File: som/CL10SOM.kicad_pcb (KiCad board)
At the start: 4 copper layers, 34 x 32 mm, 54 parts, among them IC1 10CL025YU256C8G, J1 Conn_01x02_Pin, U1 MT46H32M16LFBF-5 IT:C, U2 MX25L12833FM2, U6 AT93C46DN-SH-T, U7 SG3225CAN 50.0000M-TJGA6, X1 DF40C-120DS-0.4V51

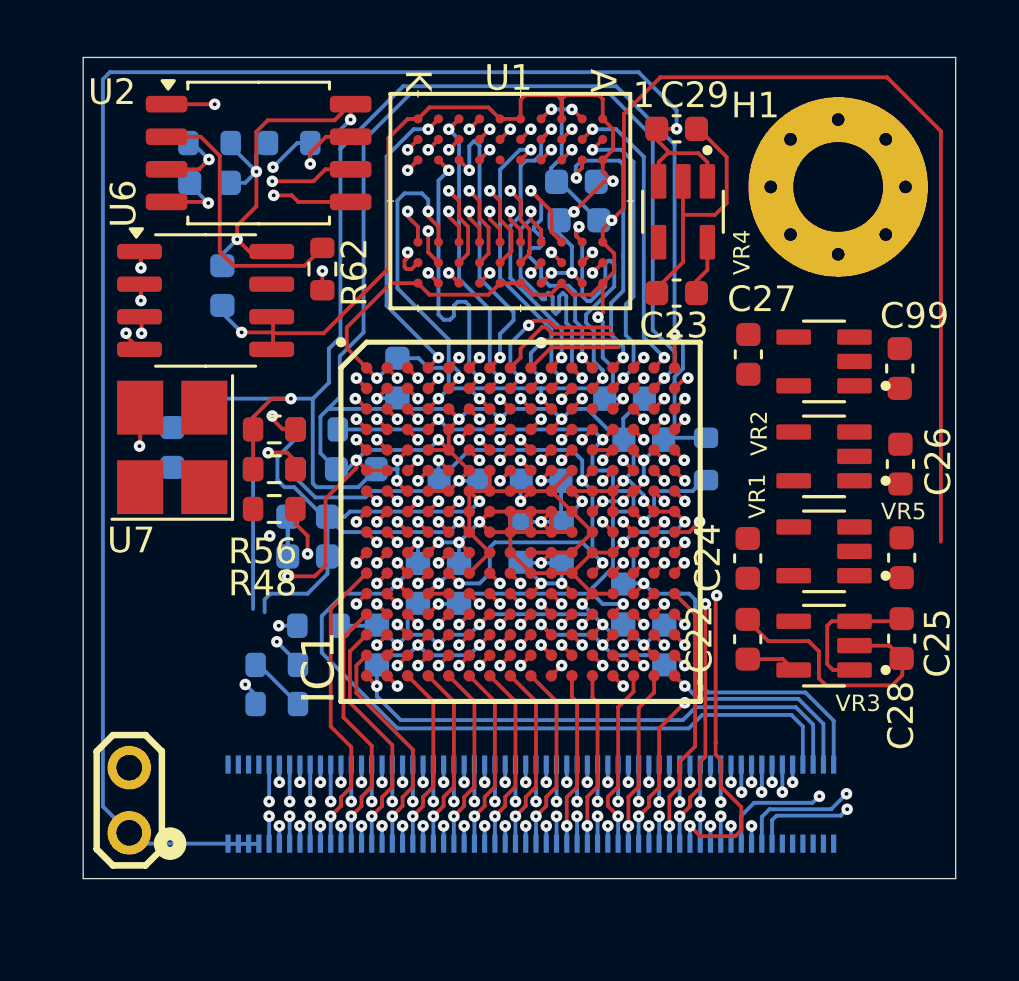
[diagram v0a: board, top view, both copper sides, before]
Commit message: Use switching regulators for 3v3 and 1v2
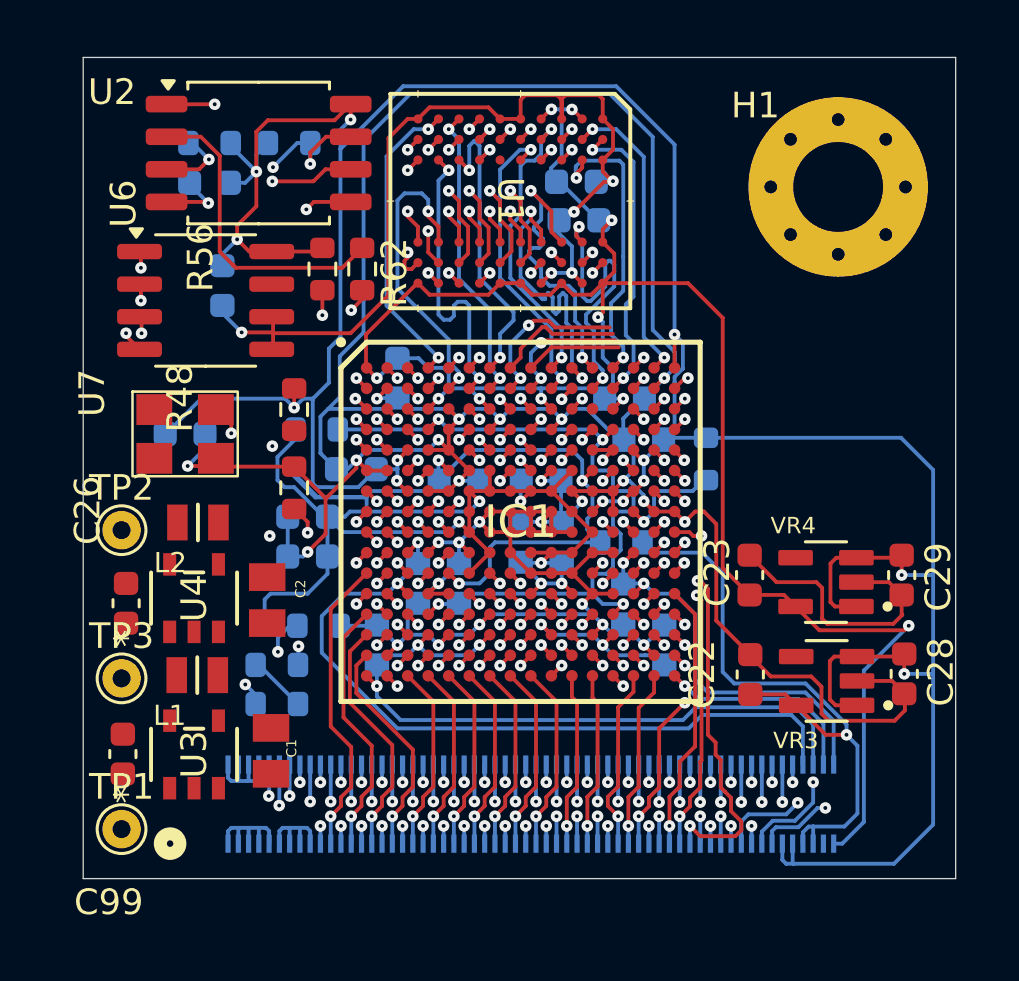
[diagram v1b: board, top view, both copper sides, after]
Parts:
- removed C24, C25, C27: 2.2uF, Capacitor_SMD:C_0603_1608Metric
- removed J1: Conn_01x02_Pin, Library:JUMPER_1
- removed VR1, VR5: AP7366EA-33W5-7, Library:SOT95P285X140-5N
- removed VR2: AP7366EA-12W5-7, Library:SOT95P285X140-5N
- added C1: GRM21BR60J226ME39L, Library:CAPC2012X140N, F.Cu at (90.6, 71.4)
- added C2: GRM21BR60J226ME39L, Library:CAPC2012X140N, F.Cu at (90.5, 65.5)
- added L1: MURATA_DFE21CCN1R0MELL, Library:MURATA_DFE21CCN1R0MELL_0, F.Cu at (87.8, 68.5)
- added L2: MURATA_DFE21CCN1R0MELL, Library:MURATA_DFE21CCN1R0MELL_0, F.Cu at (87.8, 62.5)
- added TP1: TestPoint, TestPoint:TestPoint_THTPad_D1.5mm_Drill0.7mm, F.Cu at (84.8, 74.5)
- added TP2: TestPoint, TestPoint:TestPoint_THTPad_D1.5mm_Drill0.7mm, F.Cu at (84.8, 62.8)
- added TP3: TestPoint, TestPoint:TestPoint_THTPad_D1.5mm_Drill0.7mm, F.Cu at (84.8, 68.6)
- added U3: SC189ZSKTRT, Library:SOT23-5-SC189_SEM, F.Cu at (87.6, 71.6)
- added U4: SC189CSKTRT, Library:SOT_CSKTRT_SEM, F.Cu at (87.6, 65.5)
- C26, C99: value 2.2uF -> 4.7uF
- moved C99 32.3 mm to (84.8, 71.5), turned to -90 degrees
- moved C26 31.5 mm to (85.0, 65.7), turned to -90 degrees
- moved C29 19.5 mm to (115.2, 64.6), turned to 90 degrees
- moved VR4 15.5 mm to (112.2, 64.8), turned to 180 degrees
- moved R44 13.8 mm to (104.3, 63.3), turned to 180 degrees
- moved C23 11.4 mm to (109.3, 64.6), turned to -90 degrees
- moved R56 6.53 mm to (92.6, 52.6), turned to -90 degrees
- moved R48 2.45 mm to (91.5, 58.1), turned to -90 degrees
- moved R62 1.55 mm to (94.2, 52.6)
- moved VR3 1.38 mm to (112.3, 68.7)
- moved C22 1.38 mm to (109.3, 68.5)
- moved C28 1.38 mm to (115.3, 68.4)
- moved R46 1.13 mm to (91.5, 61.2), turned to -90 degrees
- moved C9 0.73 mm to (87.3, 59.1), turned to 180 degrees
- moved U7 0.72 mm to (87.3, 59.1), turned to 0 degrees
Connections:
- C26 pad 2: Net-(VR1-OUT) -> +5V
- C28 pad 2: +5V -> +3V3
- C29 pad 2: +5V -> +3V3
- VR3 pad 1: +5V -> +3V3
- VR3 pad 3: +5V -> +3V3
- VR4 pad 1: +5V -> +3V3
- VR4 pad 3: +5V -> +3V3
- X1 pad 10: /TCK -> /TDI
- X1 pad 109: +3.3V -> +3V3
- X1 pad 11: /TMS -> +3V3
- X1 pad 111: +3.3V -> +3V3
- X1 pad 12: /TDO -> /TCK
- X1 pad 13: unconnected-(X1-Pad13) -> +3V3
- X1 pad 14: unconnected-(X1-Pad14) -> /TMS
- X1 pad 15: unconnected-(X1-Pad15) -> +3V3
- X1 pad 16: unconnected-(X1-Pad16) -> /TDO
- X1 pad 17: unconnected-(X1-Pad17) -> +3V3
- X1 pad 9: /TDI -> +5V
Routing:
- net +5V: track 70.0 -> 4.54 mm, vias 1 -> 0
- net +3V3: track 82.9 -> 131.8 mm, vias 11 -> 13
- net +2V5: track 7.42 -> 24.7 mm, vias 0 -> 1
- net GND: track 206.1 -> 219.2 mm
- net /B5-IO7p: track 18.7 -> 13.6 mm
- net /B5-IO8p: track 19.7 -> 14.7 mm
- net /B5-IO9n: track 20.5 -> 15.5 mm
- net /B5-IO7n: track 17.6 -> 12.8 mm
- net /B5-IO8n: track 19.3 -> 14.7 mm
- net +1V8: track 80.1 -> 75.8 mm, vias 9 -> 10
- net /CLC50: track 11.8 -> 7.80 mm
- net /B5-IO10: track 24.0 -> 20.8 mm
- net PLLA: track 26.6 -> 29.7 mm
- net /B5-IO11: track 26.3 -> 23.2 mm
- net /B6-IO7: track 21.4 -> 18.4 mm
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
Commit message: All routed, no errors
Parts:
- added C10: 100nF, Capacitor_SMD:C_0603_1608Metric, B.Cu at (110.7, 55.6)
- added C19: 100nF, Capacitor_SMD:C_0603_1608Metric, F.Cu at (108.8, 68.0)
- added C24: 100nF, Capacitor_SMD:C_0603_1608Metric, F.Cu at (110.3, 68.0)
- added C25: 100nF, Capacitor_SMD:C_0603_1608Metric, F.Cu at (111.8, 68.0)
- added C27: 100nF, Capacitor_SMD:C_0603_1608Metric, F.Cu at (113.4, 68.0)
- added TP4: TestPoint, TestPoint:TestPoint_THTPad_D1.5mm_Drill0.7mm, F.Cu at (85.8, 61.2)
- added TP5: TestPoint, TestPoint:TestPoint_THTPad_D1.5mm_Drill0.7mm, F.Cu at (113.2, 73.0)
- added TP6: TestPoint, TestPoint:TestPoint_THTPad_D1.5mm_Drill0.7mm, F.Cu at (112.8, 57.0)
- added U8: SG3225CAN 50.0000M-TJGA6, Library:SG3225CAN, F.Cu at (109.7, 55.6)
- C22, C23, R48, R56, R62: moved to B.Cu
- moved TP1 34.5 mm to (112.8, 54.2)
- moved TP2 10.7 mm to (85.2, 73.5)
- moved C28 7.50 mm to (108.8, 64.7), turned to -90 degrees
- moved C29 7.46 mm to (108.8, 60.8), turned to -90 degrees
- moved C23 5.93 mm to (112.3, 59.5), turned to 0 degrees
- moved C22 5.87 mm to (112.3, 63.4), turned to 0 degrees
- moved VR4 4.39 mm to (111.7, 60.5), turned to 0 degrees
- moved C45 4.38 mm to (89.6, 58.6), turned to -90 degrees
- moved VR3 4.29 mm to (111.7, 64.5), turned to 0 degrees
- moved H1 2.03 mm to (110.8, 49.0)
- moved X1 1.80 mm to (99.2, 72.5)
- moved R48 1.78 mm to (91.8, 56.4), turned to 0 degrees
- moved TP3 1.51 mm to (85.8, 67.4)
- moved L1 1.42 mm to (88.7, 67.4)
- moved L2 1.41 mm to (88.7, 61.4)
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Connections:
- IC1 pad A8: /B8-CLK10 -> GND
- IC1 pad A9: /B7-CLK8 -> /CLCOPT
- IC1 pad B8: /B8-CLK11 -> GND
- IC1 pad B9: /B7-CLK9 -> GND
- IC1 pad N8: /B3-IO15 -> /B3-IO16
- IC1 pad P8: /B3-IO16 -> /B3-IO17
- X1 pad 109: +3V3 -> +2V5
- X1 pad 111: +3V3 -> +2V5
- X1 pad 113: +2V5 -> +1V8
- X1 pad 115: +2V5 -> +1V8
- X1 pad 117: +1V8 -> +3V3
- X1 pad 119: +1V8 -> +3V3
- X1 pad 17: +3V3 -> +2V5
- X1 pad 54: /B3-IO15 -> /B3-IO16
- X1 pad 56: /B3-IO16 -> /B3-IO17
- X1 pad 9: +5V -> +3V3
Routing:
- net GND: track 219.2 -> 327.3 mm, vias 34 -> 43
- net +3V3: track 131.8 -> 203.6 mm, vias 13 -> 17
- net +2V5: track 24.7 -> 54.3 mm, vias 1 -> 4
- net +5V: track 4.54 -> 28.8 mm, vias 0 -> 2
- net +1V2: track 44.0 -> 58.0 mm, vias 6 -> 10
- net /CLCOPT: track 0.00 -> 10.2 mm
- net PLLA: track 29.7 -> 20.2 mm
- net /B3-IO15: track 18.1 -> 9.20 mm, vias 4 -> 2
- net /B3-IO17: track 0.00 -> 7.39 mm, vias 0 -> 2
- net /B8-CLK11: track 6.54 -> 0.00 mm, vias 2 -> 0
- net +1V8: track 75.8 -> 81.9 mm, vias 10 -> 14
- net /B7-CLK9: track 5.22 -> 0.00 mm, vias 2 -> 0
- net /B8-CLK10: track 4.96 -> 0.00 mm
- net /TDO: track 14.1 -> 17.9 mm
- net /B7-CLK8: track 3.76 -> 0.00 mm
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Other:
- board size 34 x 32 mm -> 31 x 30.5 mm

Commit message: Fixed warnings
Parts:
- removed TP2: TestPoint, TestPoint:TestPoint_THTPad_D1.5mm_Drill0.7mm
- TP1, TP3, TP4, TP5, TP6: footprint TestPoint:TestPoint_THTPad_D1.5mm_Drill0.7mm -> TestPoint:TestPoint_THTPad_D1.0mm_Drill0.5mm
- moved TP1 0.53 mm to (113.3, 54.3)
- moved TP6 0.50 mm to (113.2, 57.0)
- moved TP5 0.47 mm to (113.7, 73.2)
- moved C99 0.37 mm to (84.8, 70.3)
- moved TP3 0.10 mm to (85.8, 67.5)
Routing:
- net +5V: track 28.8 -> 24.7 mm
- net GND: track 327.3 -> 324.0 mm, vias 43 -> 42
- net +2V5: track 54.3 -> 54.8 mm

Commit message: Improvements
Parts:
- H1: footprint MountingHole:MountingHole_3.5mm_Pad_Via -> MountingHole:MountingHole_2.7mm_M2.5_Pad_Via
- moved H1 1.12 mm to (111.2, 48.0)
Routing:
- net /B3-IO1n: track 8.05 -> 10.2 mm
- net /B2-IO1p: track 12.2 -> 13.7 mm
- net /B2-IO2n: track 12.4 -> 13.7 mm
- net /B2-IO5n: track 9.69 -> 10.9 mm
- net GND: track 324.0 -> 325.0 mm
- net /B2-IO3n: track 11.5 -> 12.5 mm
- net /DDR_DQ15: track 11.0 -> 11.8 mm
- net /DDR_DM1: track 13.9 -> 14.6 mm

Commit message: Improvements
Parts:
- L1, L2: value MURATA_DFE21CCN1R0MELL -> DFE21CCN1R0MELL
- R62: value 25E -> 24E9

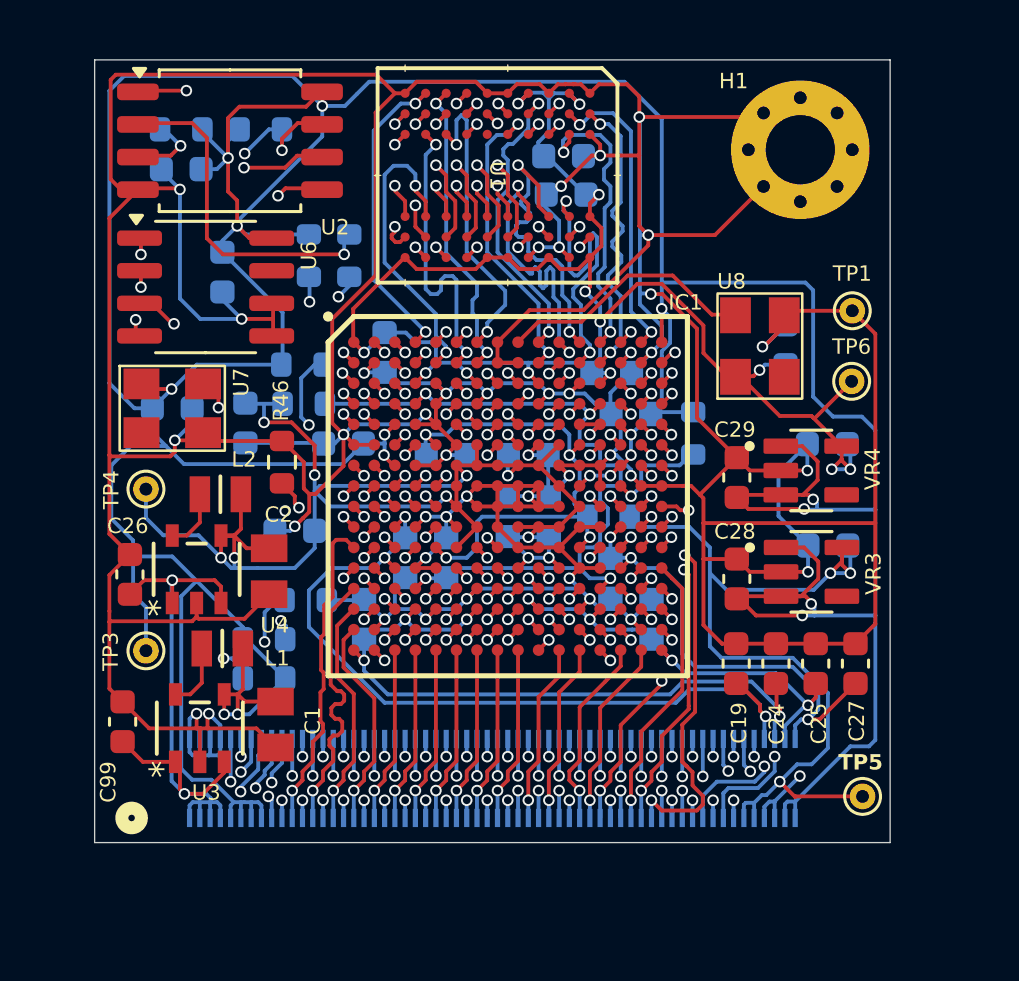
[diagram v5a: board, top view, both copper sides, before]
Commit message: Use differential routing
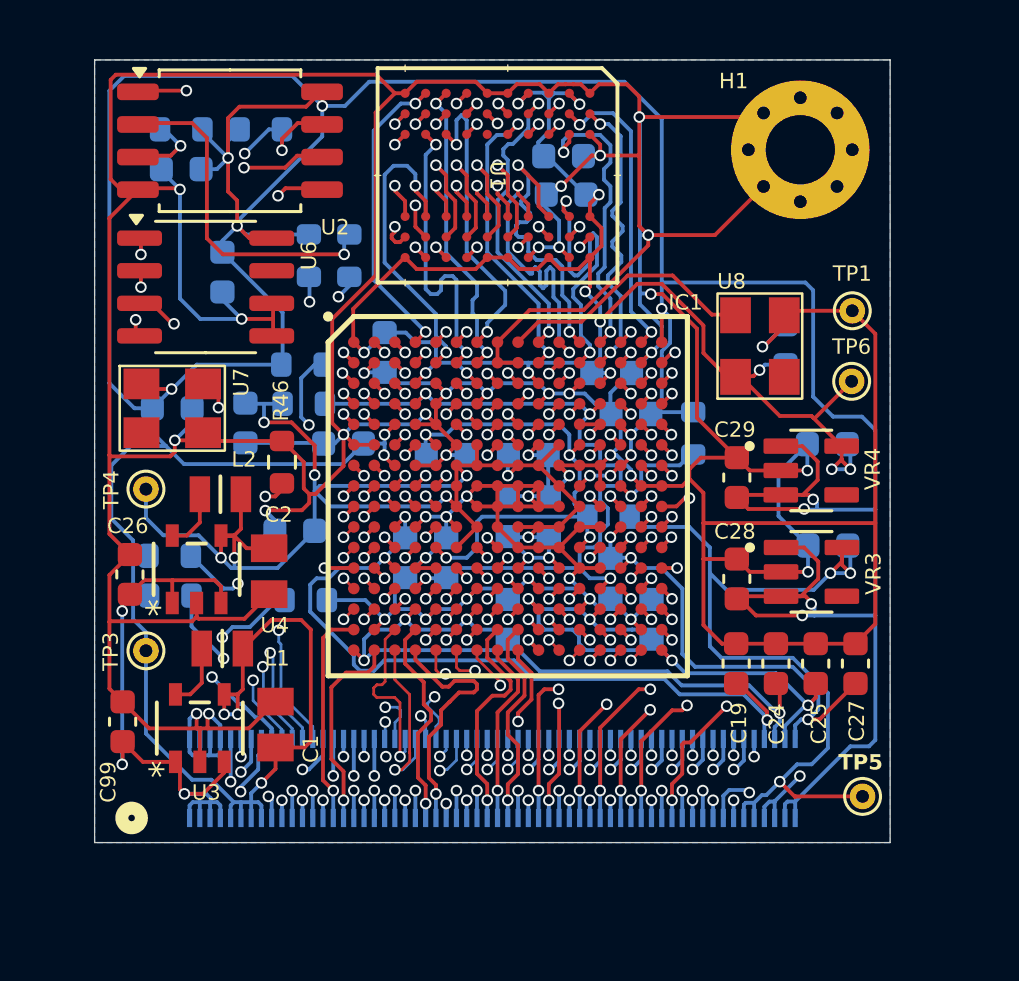
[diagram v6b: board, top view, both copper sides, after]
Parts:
- moved C20 5.60 mm to (99.8, 66.3)
- moved R58 4.91 mm to (86.7, 63.8)
- moved R59 4.87 mm to (86.7, 65.4), turned to 0 degrees
- turned C1 to 90 degrees
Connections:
- net /B6-IO8p renamed /B6-IO10
- IC1 pad B16: /B6-IO4 -> /B6-IO5
- IC1 pad C16: /B6-IO8n -> /B6-IO9
- IC1 pad D15: /B6-IO7 -> /B6-IO8
- IC1 pad D16: /B6-IO6 -> /B6-IO7
- IC1 pad F14: /B6-IO5 -> /B6-IO6
- IC1 pad F15: /B6-IO3p -> /B6-IO4
- IC1 pad F16: /B6-IO3n -> /B6-IO3
- IC1 pad G15: /B6-IO1p -> /B6-IO1P
- IC1 pad G16: /B6-IO1n -> /B6-IO1N
- IC1 pad J1: /B2-IO1n -> /B2-IO1N
- IC1 pad J15: /B5-IO9p -> /B5-IO9P
- IC1 pad J16: /B5-IO9n -> /B5-IO9N
- IC1 pad J2: /B2-IO1p -> /B2-IO1P
- IC1 pad K1: /B2-IO2n -> /B2-IO2N
- IC1 pad K15: /B5-IO8p -> /B5-IO8P
- IC1 pad K16: /B5-IO8n -> /B5-IO8N
- IC1 pad K2: /B2-IO2p -> /B2-IO2P
- IC1 pad L1: /B2-IO3n -> /B2-IO3N
- IC1 pad L15: /B5-IO7p -> /B5-IO7P
- IC1 pad L16: /B5-IO7n -> /B5-IO7N
- IC1 pad L2: /B2-IO3p -> /B2-IO3P
- IC1 pad N1: /B2-IO5n -> /B2-IO5N
- IC1 pad N15: /B5-IO4p -> /B5-IO4P
- IC1 pad N16: /B5-IO4n -> /B5-IO4N
- IC1 pad N2: /B2-IO5p -> /B2-IO5P
- IC1 pad N3: /B3-IO1p -> /B3-IO1P
- IC1 pad N5: /B3-IO6p -> /B3-IO6P
- IC1 pad N6: /B3-IO6n -> /B3-IO6N
- IC1 pad P1: /B2-IO9n -> /B2-IO9N
- IC1 pad P14: /B4-IO12-COp -> /B4-IO12-COP
- IC1 pad P16: /B5-IO3n -> /B5-IO3N
- IC1 pad P2: /B2-IO9p -> /B2-IO9P
- IC1 pad P3: /B3-IO1n -> /B3-IO1N
- IC1 pad R10: /B4-IO2p -> /B4-IO2P
- IC1 pad R11: /B4-IO3p -> /B4-IO3P
- IC1 pad R12: /B4-IO4p -> /B4-IO4P
- IC1 pad R13: /B4-IO7p -> /B4-IO7P
- IC1 pad R14: /B4-IO12-COn -> /B4-IO12-CON
- IC1 pad R16: /B5-IO3p -> /B5-IO3P
- IC1 pad R3: /B3-IO2p -> /B3-IO2P
- IC1 pad R4: /B3-IO4-COp -> /B3-IO4-COP
- IC1 pad R5: /B3-IO10p -> /B3-IO10P
- IC1 pad R6: /B3-IO11p -> /B3-IO11P
- IC1 pad R7: /B3-IO13p -> /B3-IO13P
- IC1 pad T10: /B4-IO2n -> /B4-IO2N
- IC1 pad T11: /B4-IO3n -> /B4-IO3N
- IC1 pad T12: /B4-IO4n -> /B4-IO4N
- IC1 pad T13: /B4-IO7n -> /B4-IO7N
- IC1 pad T14: /B4-IO10p -> /B4-IO10P
- IC1 pad T15: /B4-IO10n -> /B4-IO10N
- IC1 pad T3: /B3-IO2n -> /B3-IO2N
- IC1 pad T4: /B3-IO5-COn -> /B3-IO4-CON
- IC1 pad T5: /B3-IO10n -> /B3-IO10N
- IC1 pad T6: /B3-IO11n -> /B3-IO11N
- IC1 pad T7: /B3-IO13n -> /B3-IO13N
- X1 pad 100: /B6-CLK4 -> /B5-IO8P
- X1 pad 101: /B5-IO9p -> /B6-IO8
- X1 pad 102: /B6-IO4 -> /B5-IO8N
- X1 pad 103: /B5-IO9n -> /B6-IO7
- X1 pad 104: /B6-IO5 -> /B5-IO9P
- X1 pad 105: /B5-IO10 -> /B6-IO5
- X1 pad 106: /B6-IO6 -> /B5-IO9N
- X1 pad 107: /B5-IO11 -> /B6-IO9
- X1 pad 108: /B6-IO7 -> /B6-IO1P
- X1 pad 110: /B6-IO8n -> /B6-IO1N
- X1 pad 19: /B2-IO3p -> /B2-IO6
- X1 pad 20: /B2-IO2p -> /B2-IO1N
- X1 pad 21: /B2-IO3n -> /B2-IO4
- X1 pad 22: /B2-IO2n -> /B2-IO1P
- X1 pad 23: /B2-IO5p -> /B2-CLK3
- X1 pad 24: /B2-IO1p -> /B2-IO2N
- X1 pad 25: /B2-IO5n -> /B2-CLK2
- X1 pad 26: /B2-IO1n -> /B2-IO2P
- X1 pad 27: /B2-IO9p -> /B2-IO7
- X1 pad 28: /B2-CLK2 -> /B2-IO3N
- X1 pad 29: /B2-IO9n -> /B2-IO8
- X1 pad 30: /B2-CLK3 -> /B2-IO3P
- X1 pad 31: /B2-IO7 -> /B3-IO3
- X1 pad 32: /B2-IO6 -> /B2-IO5N
- X1 pad 33: /B2-IO8 -> /B3-IO14
- X1 pad 34: /B2-IO4 -> /B2-IO5P
- X1 pad 35: /B3-IO2p -> /B3-IO12
- X1 pad 36: /B3-IO3 -> /B2-IO9N
- X1 pad 37: /B3-IO2n -> /B3-IO7
- X1 pad 38: /B3-IO1p -> /B2-IO9P
- X1 pad 39: /B3-IO4-COp -> /B3-IO8
- X1 pad 40: /B3-IO1n -> /B3-IO1P
- X1 pad 41: /B3-IO5-COn -> /B3-IO9
- X1 pad 42: /B3-IO6p -> /B3-IO1N
- X1 pad 43: /B3-IO10p -> /B3-IO16
- X1 pad 44: /B3-IO6n -> /B3-IO2P
- X1 pad 45: /B3-IO10n -> /B3-IO17
- X1 pad 46: /B3-IO8 -> /B3-IO2N
- X1 pad 47: /B3-IO11p -> /B3-IO4-COP
- X1 pad 48: /B3-IO12 -> /B3-IO6P
- X1 pad 49: /B3-IO11n -> /B3-IO4-CON
- X1 pad 50: /B3-IO7 -> /B3-IO6N
- X1 pad 51: /B3-IO13p -> /B3-IO15
- X1 pad 52: /B3-IO9 -> /B3-IO10P
- X1 pad 53: /B3-IO13n -> /B4-IO5
- X1 pad 54: /B3-IO16 -> /B3-IO10N
- X1 pad 55: /B3-CLK15 -> /B4-IO1
- X1 pad 56: /B3-IO17 -> /B3-IO11P
- X1 pad 57: /B3-CLK14 -> /B4-IO8
- X1 pad 58: /B4-IO1 -> /B3-IO11N
- X1 pad 59: /B4-CLK13 -> /B3-CLK15
- X1 pad 60: /B3-IO15 -> /B3-IO13P
- X1 pad 61: /B4-CLK12 -> /B3-CLK14
- X1 pad 62: /B3-IO14 -> /B3-IO13N
- X1 pad 63: /B4-IO8 -> /B4-CLK13
- X1 pad 64: /B4-IO9 -> /B4-IO2P
- X1 pad 65: /B4-IO3p -> /B4-CLK12
- X1 pad 66: /B4-IO2p -> /B4-IO2N
- X1 pad 67: /B4-IO3n -> /B4-IO9
- X1 pad 68: /B4-IO2n -> /B4-IO3P
- X1 pad 69: /B4-IO4p -> /B4-IO6
- X1 pad 70: /B4-IO5 -> /B4-IO3N
- X1 pad 71: /B4-IO4n -> /B4-IO11
- X1 pad 72: /B4-IO6 -> /B4-IO4P
- X1 pad 73: /B4-IO12-COp -> /B5-IO6
- X1 pad 74: /B4-IO7p -> /B4-IO4N
- X1 pad 75: /B4-IO12-COn -> /B5-IO1
- X1 pad 76: /B4-IO7n -> /B4-IO7P
- X1 pad 77: /B4-IO10p -> /B5-IO2
- X1 pad 78: /B4-IO11 -> /B4-IO7N
- X1 pad 79: /B4-IO10n -> /B5-CLK6
- X1 pad 80: /B5-IO1 -> /B4-IO10P
- X1 pad 81: /B5-IO2 -> /B5-CLK7
- X1 pad 82: /B5-IO4n -> /B4-IO10N
- X1 pad 83: /B5-IO3p -> /B5-IO5
- X1 pad 84: /B5-IO4p -> /B4-IO12-COP
- X1 pad 85: /B5-IO3n -> /B5-IO11
- X1 pad 86: /B5-IO5 -> /B4-IO12-CON
- X1 pad 87: /B5-CLK7 -> /B5-IO10
- X1 pad 88: /B6-IO1p -> /B5-IO4P
- X1 pad 89: /B5-CLK6 -> /B6-IO2
- X1 pad 90: /B6-IO1n -> /B5-IO4N
- X1 pad 91: /B5-IO6 -> /B6-IO6
- X1 pad 92: /B6-IO2 -> /B5-IO3P
- X1 pad 93: /B5-IO7p -> /B6-IO3
- X1 pad 94: /B6-IO3n -> /B5-IO3N
- X1 pad 95: /B5-IO7n -> /B6-IO4
- X1 pad 96: /B6-IO3p -> /B5-IO7P
- X1 pad 97: /B5-IO8p -> /B6-CLK5
- X1 pad 98: /B6-CLK5 -> /B5-IO7N
- X1 pad 99: /B5-IO8n -> /B6-CLK4
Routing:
- net /B6-IO9: track 0.00 -> 21.0 mm, vias 0 -> 2
- net /B6-IO8n: track 19.7 -> 0.00 mm, vias 2 -> 0
- net /B6-IO8: track 0.00 -> 19.7 mm, vias 0 -> 2
- net /B5-IO9p: track 18.2 -> 0.00 mm, vias 2 -> 0
- net /B6-IO1N: track 0.00 -> 18.0 mm, vias 0 -> 2
- net /B6-IO1P: track 0.00 -> 18.0 mm, vias 0 -> 2
- net /B6-IO3: track 0.00 -> 16.9 mm, vias 0 -> 2
- net /B6-IO3n: track 16.5 -> 0.00 mm, vias 2 -> 0
- net /B6-IO3p: track 16.4 -> 0.00 mm, vias 2 -> 0
- net /B5-IO9P: track 0.00 -> 15.7 mm, vias 0 -> 2
- net /B6-IO1n: track 15.6 -> 0.00 mm, vias 2 -> 0
- net /B5-IO9N: track 0.00 -> 15.6 mm, vias 0 -> 2
- net /B5-IO8P: track 0.00 -> 15.5 mm, vias 0 -> 2
- net /B5-IO8N: track 0.00 -> 15.5 mm, vias 0 -> 2
- net /B5-IO4N: track 0.00 -> 15.3 mm, vias 0 -> 2
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- added copper zone on B.Cu, net GND
